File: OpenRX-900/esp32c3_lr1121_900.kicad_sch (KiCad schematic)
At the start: 39 parts, among them U1 ESP32-C3FH4, U2 TLV75533PDQNR, U3 SX1281IMLTRT, U4 RFX2401C, X1 CJ17-400001010B20

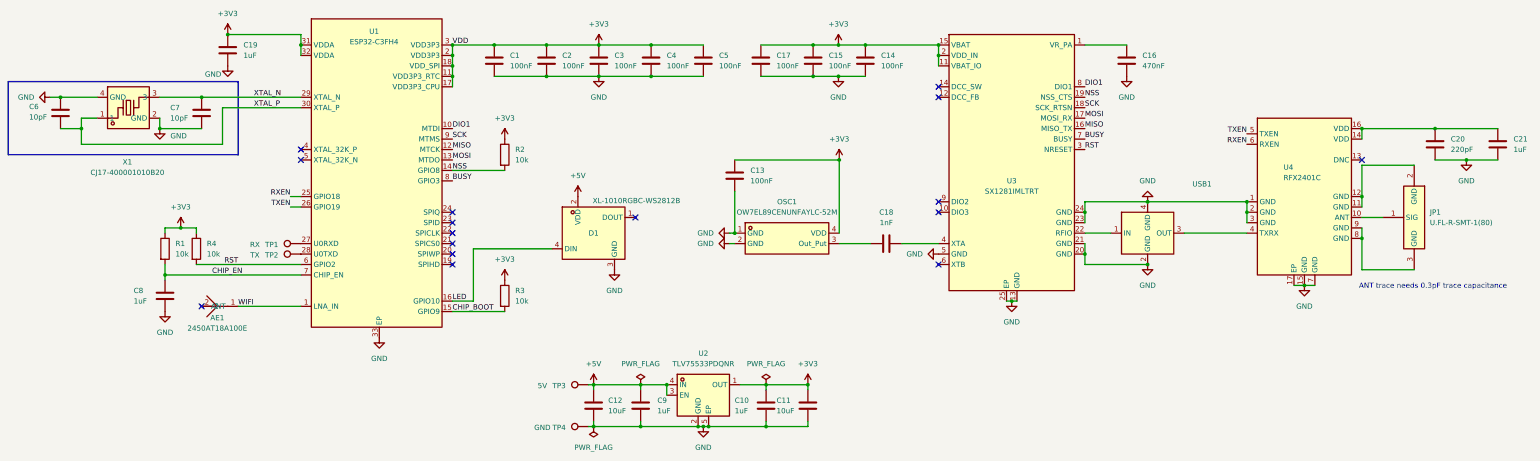
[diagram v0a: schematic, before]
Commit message: OpenRX-900: add all LCSC fields, fix 4.7uF to 0402
- C20 (4.7uF): C23733, footprint fixed from 0201 to 0402
- R5/R6/R7 (100k): C25741, RFSW pull-downs
- L1 (10uH): C1035, 0603 DC-DC inductor
- U4 (LR1121): C7498014
- U5 (32MHz TCXO): C22434888
- T1 (Johanson IPD): C19842466
- JP1 (UFL): C88374
- 0 ERC errors, all components have LCSC fields
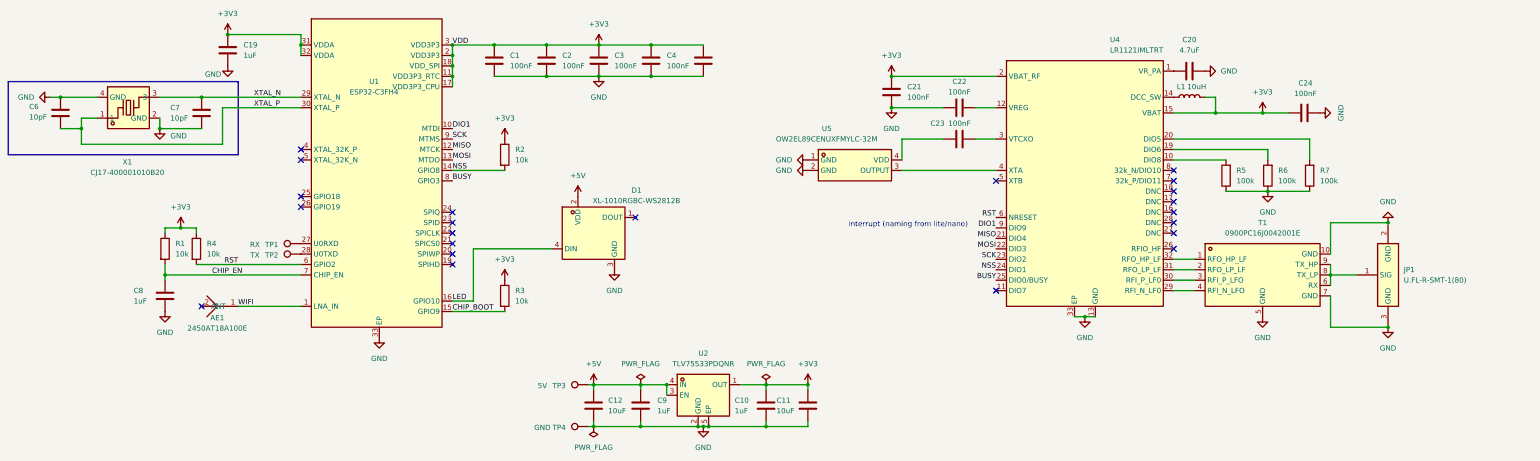
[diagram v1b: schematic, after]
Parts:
- removed C13, C14, C15, C17: 100nF, Capacitor_SMD:C_0201_0603Metric, symbol Device:C
- removed C16: 470nF, Capacitor_SMD:C_0201_0603Metric, symbol Device:C
- removed C18: 1nF, Capacitor_SMD:C_0201_0603Metric, symbol Device:C
- removed OSC1: OW7EL89CENUNFAYLC-52M, OpenRX-Shared:OSC-SMD_4P-L2.0-W1.6-BL_TXC_7Z, symbol OpenRX-Shared:OW7EL89CENUNFAYLC-52M
- removed U3: SX1281IMLTRT, OpenRX-Shared:QFN-24_L4.0-W4.0-P0.50-TL-EP2.6, symbol OpenRX-Shared:SX1281IMLTRT
- removed U4: RFX2401C, OpenRX-Shared:QFN-16_L3.0-W3.0-P0.50-BL-EP1.7, symbol OpenRX-Shared:RFX2401C
- removed USB1: DEA102700LT-6307A2, OpenRX-Shared:FILTER-SMD_4P-L1.0-W0.5-L_DEA102700LT-XXX, symbol OpenRX-Shared:DEA102700LT-6307A2
- added C22, C23, C24: 100nF, Capacitor_SMD:C_0201_0603Metric, symbol Device:C
- added L1: 10uH, Inductor_SMD:L_0603_1608Metric, symbol Device:L
- added R5, R6, R7: 100k, Resistor_SMD:R_0201_0603Metric, symbol Device:R
- added T1: 0900PC16J0042001E, OpenRX-Shared:FILTER-SMD_10P-L2.0-W1.6-BL, symbol OpenRX-Shared:0900PC16J0042001E
- added U4: LR1121IMLTRT, OpenRX-Shared:QFN-32_L5.0-W5.0-P0.50-BL-EP3.7, symbol OpenRX-Shared:LR1121IMLTRT
- added U5: OW2EL89CENUXFMYLC-32M, OpenRX-Shared:OSC-SMD_4P-L3.2-W2.5-BL, symbol OpenRX-Shared:OW2EL89CENUXFMYLC-32M
- C20: value 220pF -> 4.7uF; footprint Capacitor_SMD:C_0201_0603Metric -> Capacitor_SMD:C_0402_1005Metric; LCSC C14856 -> C23733
- C21: value 1uF -> 100nF; LCSC C77857 -> C14858
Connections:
- net +3V3: now also C21.1, C24.2, L1.2, U4.15 (VBAT), U4.2 (VBAT_RF)
- net BUSY: now also U4.25 (DIO0/BUSY)
- net DIO1: now also U4.9 (DIO9)
- net GND: now also JP1.2 (GND), JP1.3 (GND), C22.1, C24.1, R5.1, R6.1, R7.1, T1.10 (GND), T1.5 (GND), T1.7 (GND), U4.13 (GND), U4.33 (EP), U5.1 (GND), U5.2 (GND)
- net MISO: now also U4.21 (DIO4)
- net MOSI: now also U4.22 (DIO3)
- net NSS: now also U4.24 (DIO1)
- net RST: now also U4.6 (NRESET)
- net SCK: now also U4.23 (DIO2)
- net at C20.1: now also U4.1 (VR_PA); no longer C21.1
- net at JP1.1 (SIG): now also T1.6 (RX), T1.8 (TX_LP), T1.9 (TX_HP)
- net RXEN: no longer names the net of U1.25 (GPIO18)
- net TXEN: no longer names the net of U1.26 (GPIO19)
- new net: C22.2, U4.12 (VREG)
- new net: C23.1, U5.4 (VDD)
- new net: C23.2, U4.3 (VTCXO)
- new net: R5.2, U4.10 (DIO8)
- new net: L1.1, U4.14 (DCC_SW)
- new net: R6.2, U4.19 (DIO6)
- new net: R7.2, U4.20 (DIO5)
- new net: T1.4 (RFI_N_LFO), U4.29 (RFI_N_LF0)
- new net: T1.3 (RFI_P_LFO), U4.30 (RFI_P_LF0)
- new net: T1.2 (RFO_LP_LF), U4.31 (RFO_LP_LF)
- new net: T1.1 (RFO_HP_LF), U4.32 (RFO_HP_LF)
- new net: U4.4 (XTA), U5.3 (OUTPUT)
- no-connect marks 16 -> 22
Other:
- note added: "interrupt (naming from lite/nano)"
- note removed: "ANT trace needs 0.3pF trace capacitance"

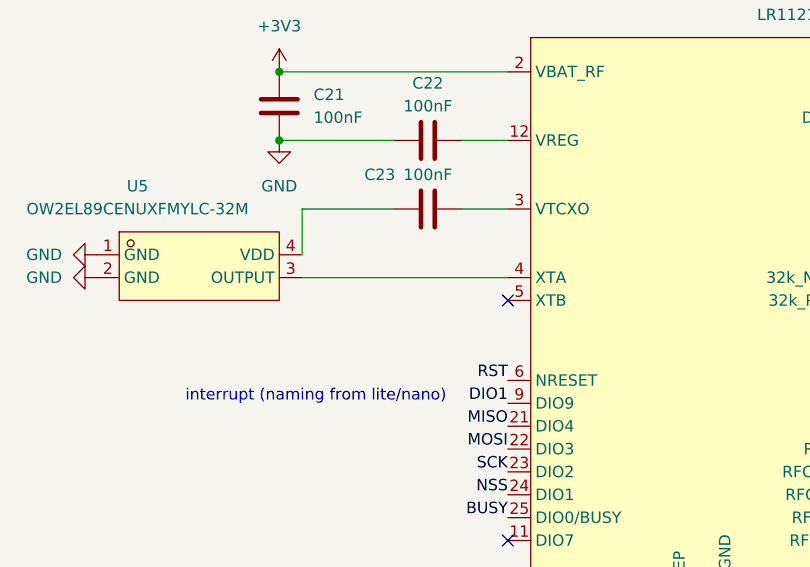
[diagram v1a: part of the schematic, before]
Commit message: Fix 220R LCSC to C25092, add TCXO series resistor to 900
- 220R 0201 1%: C25092 (was incorrectly C25741/100k)
- Both 900 and Dual now have correct 220R + 10pF on TCXO→XTA path
- Nano: RFX2401C VDD now connected to +3V3
- All 4 schematics: 0 ERC errors
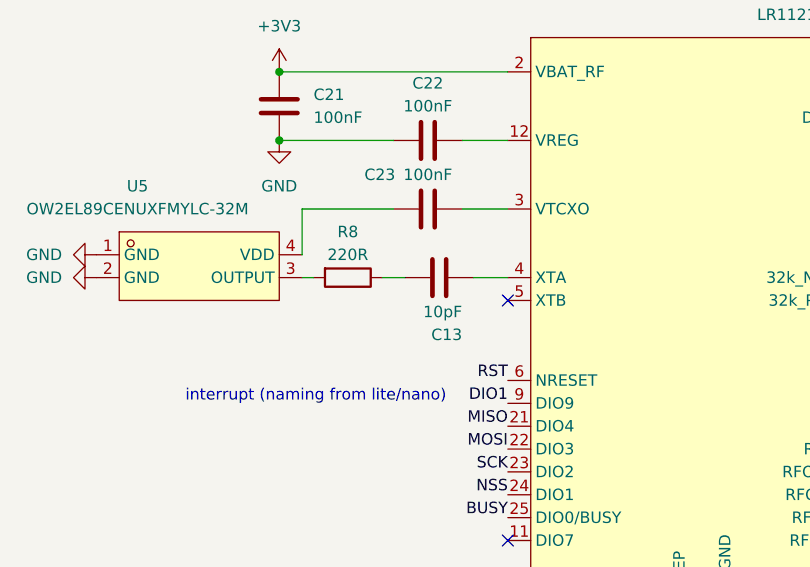
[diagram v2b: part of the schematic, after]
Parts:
- added C13: 10pF, Capacitor_SMD:C_0201_0603Metric, symbol Device:C
- added R8: 220R, Resistor_SMD:R_0201_0603Metric, symbol Device:R
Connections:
- net at U4.4 (XTA): now also C13.2; no longer U5.3 (OUTPUT)
- new net: C13.1, R8.1
- new net: R8.2, U5.3 (OUTPUT)
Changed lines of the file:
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@@
 	(wire
 		(pts
-			(xy 243.84 59.69) (xy 266.7 59.69)
-		)
-		(stroke
-			(width 0)
-			(type default)
-		)
-	)
-	(wire
-		(pts
 			(xy 309.88 86.36) (xy 314.96 86.36)
 		)
@@
 	(wire
 		(pts
+			(xy 245.11 59.69) (xy 243.84 59.69)
+		)
+		(stroke
+			(width 0)
+			(type default)
+		)
+	)
+	(wire
+		(pts
 			(xy 309.88 83.82) (xy 314.96 83.82)
 		)
@@
 	(wire
 		(pts
+			(xy 252.73 59.69) (xy 255.27 59.69)
+		)
+		(stroke
+			(width 0)
+			(type default)
+		)
+	)
+	(wire
+		(pts
 			(xy 64.77 85.09) (xy 64.77 82.55)
 		)
@@
 	(wire
 		(pts
+			(xy 262.89 59.69) (xy 266.7 59.69)
+		)
+		(stroke
+			(width 0)
+			(type default)
+		)
+	)
+	(wire
+		(pts
 			(xy 167.64 111.76) (xy 180.34 111.76)
 		)
@@
 			)
 		)
-		(pin "3"
-		)
-		(pin "2"
-		)
 		(property "LCSC" "C88374"
 			(at 0 0 0)
+			(hide yes)
 			(show_name no)
 			(do_not_autoplace no)
-			(hide yes)
 			(effects
 				(font
@@
 			)
 		)
+		(pin "3"
+		)
+		(pin "2"
+		)
 		(pin "1"
 		)
@@
 			)
 		)
-		(pin "2"
-		)
-		(pin "6"
-		)
-		(pin "7"
-		)
-		(pin "9"
-		)
-		(pin "5"
-		)
 		(property "LCSC" "C7498014"
 			(at 0 0 0)
+			(hide yes)
 			(show_name no)
 			(do_not_autoplace no)
-			(hide yes)
 			(effects
 				(font
@@
 			)
 		)
+		(pin "2"
+		)
+		(pin "6"
+		)
+		(pin "7"
+		)
+		(pin "9"
+		)
+		(pin "5"
+		)
 		(pin "1"
 		)
@@
 		(property "LCSC" "C23733"
 			(at 0 0 0)
+			(hide yes)
 			(show_name no)
 			(do_not_autoplace no)
-			(hide yes)
 			(effects
 				(font
@@
 	)
 	(symbol
+		(lib_id "Device:C")
+		(at 259.08 59.69 90)
+		(unit 1)
+		(body_style 1)
+		(exclude_from_sim no)
+		(in_bom yes)
+		(on_board yes)
+		(in_pos_files yes)
+		(dnp no)
+		(property "Reference" "C13"
+			(at 261.62 66.04 90)
+			(show_name no)
+			(do_not_autoplace no)
+			(effects
+				(font
+					(size 1.27 1.27)
+				)
+				(justify left)
+			)
+		)
+		(property "Value" "10pF"
+			(at 261.62 63.5 90)
+			(show_name no)
+			(do_not_autoplace no)
+			(effects
+				(font
+					(size 1.27 1.27)
+				)
+				(justify left)
+			)
+		)
+		(property "Footprint" "Capacitor_SMD:C_0201_0603Metric"
+			(at 262.89 58.7248 0)
+			(hide yes)
+			(show_name no)
+			(do_not_autoplace no)
+			(effects
+				(font
+					(size 1.27 1.27)
+				)
+			)
+		)
+		(property "Datasheet" ""
+			(at 259.08 59.69 0)
+			(hide yes)
+			(show_name no)
+			(do_not_autoplace no)
+			(effects
+				(font
+					(size 1.27 1.27)
+				)
+			)
+		)
+		(property "Description" "Unpolarized capacitor"
+			(at 259.08 59.69 0)
+			(hide yes)
+			(show_name no)
+			(do_not_autoplace no)
+			(effects
+				(font
+					(size 1.27 1.27)
+				)
+			)
+		)
+		(property "LCSC" "C14854"
+			(at 213.36 133.35 0)
+			(hide yes)
+			(show_name no)
+			(do_not_autoplace no)
+			(effects
+				(font
+					(size 1.27 1.27)
+				)
+			)
+		)
+		(pin "1"
+		)
+		(pin "2"
+		)
+		(instances
+			(project "OpenRX-900"
+				(path "/a1b2c3d4-e5f6-7890-abcd-ef1234567890/e1f2a3b4-c5d6-7890-1234-567890abcdef"
+					(reference "C13")
+					(unit 1)
+				)
+			)
+		)
+	)
+	(symbol
 		(lib_id "power:GND")
 		(at 331.47 95.25 0)
@@
 			)
 		)
-		(pin "4"
-		)
-		(pin "3"
-		)
 		(property "LCSC" "C22434888"
 			(at 0 0 0)
+			(hide yes)
 			(show_name no)
 			(do_not_autoplace no)
-			(hide yes)
 			(effects
 				(font
@@
 			)
 		)
+		(pin "4"
+		)
+		(pin "3"
+		)
 		(pin "1"
 		)
@@
 			)
 		)
+		(property "LCSC" "C1035"
+			(at 0 0 0)
+			(hide yes)
+			(show_name no)
+			(do_not_autoplace no)
+			(effects
+				(font
+					(size 1.27 1.27)
+				)
+			)
+		)
 		(pin "2"
 		)
-		(property "LCSC" "C1035"
+		(pin "1"
+		)
+		(instances
+			(project "OpenRX-900"
+				(path "/a1b2c3d4-e5f6-7890-abcd-ef1234567890/e1f2a3b4-c5d6-7890-1234-567890abcdef"
+					(reference "L1")
+					(unit 1)
+				)
+			)
+		)
+	)
+	(symbol
+		(lib_id "Device:R")
+		(at 248.92 59.69 270)
+		(unit 1)
+		(body_style 1)
+		(exclude_from_sim no)
+		(in_bom yes)
+		(on_board yes)
+		(in_pos_files yes)
+		(dnp no)
+		(property "Reference" "R8"
+			(at 248.92 54.61 90)
+			(show_name no)
+			(do_not_autoplace no)
+			(effects
+				(font
+					(size 1.27 1.27)
+				)
+			)
+		)
+		(property "Value" "220R"
+			(at 248.92 57.15 90)
+			(show_name no)
+			(do_not_autoplace no)
+			(effects
+				(font
+					(size 1.27 1.27)
+				)
+			)
+		)
+		(property "Footprint" "Resistor_SMD:R_0201_0603Metric"
+			(at 248.92 57.912 90)
+			(hide yes)
+			(show_name no)
+			(do_not_autoplace no)
+			(effects
+				(font
+					(size 1.27 1.27)
+				)
+			)
+		)
+		(property "Datasheet" ""
+			(at 248.92 59.69 0)
+			(hide yes)
+			(show_name no)
+			(do_not_autoplace no)
+			(effects
+				(font
+					(size 1.27 1.27)
+				)
+			)
+		)
+		(property "Description" "Resistor"
+			(at 248.92 59.69 0)
+			(hide yes)
+			(show_name no)
+			(do_not_autoplace no)
+			(effects
+				(font
+					(size 1.27 1.27)
+				)
+			)
+		)
+		(property "LCSC" "C25092"
+			(at 187.96 382.27 0)
+			(hide yes)
+			(show_name no)
+			(do_not_autoplace no)
+			(effects
+				(font
+					(size 1.27 1.27)
+				)
+			)
+		)
+		(property "LCSC" "C25092"
 			(at 0 0 0)
 			(show_name no)
@@
 			)
 		)
+		(pin "2"
+		)
 		(pin "1"
 		)
@@
 			(project "OpenRX-900"
 				(path "/a1b2c3d4-e5f6-7890-abcd-ef1234567890/e1f2a3b4-c5d6-7890-1234-567890abcdef"
-					(reference "L1")
+					(reference "R8")
 					(unit 1)
 				)
@@
 			)
 		)
+		(property "LCSC" "C19842466"
+			(at 0 0 0)
+			(hide yes)
+			(show_name no)
+			(do_not_autoplace no)
+			(effects
+				(font
+					(size 1.27 1.27)
+				)
+			)
+		)
 		(pin "4"
 		)
@@
 		(pin "8"
 		)
-		(property "LCSC" "C19842466"
-			(at 0 0 0)
-			(show_name no)
-			(do_not_autoplace no)
-			(hide yes)
-			(effects
-				(font
-					(size 1.27 1.27)
-				)
-			)
-		)
 		(pin "1"
 		)
@@
 			)
 		)
-		(pin "2"
-		)
 		(property "LCSC" "C25741"
 			(at 0 0 0)
+			(hide yes)
 			(show_name no)
 			(do_not_autoplace no)
-			(hide yes)
 			(effects
 				(font
@@
 			)
 		)
+		(pin "2"
+		)
 		(pin "1"
 		)
@@
 			)
 		)
-		(pin "2"
-		)
 		(property "LCSC" "C25741"
 			(at 0 0 0)
+			(hide yes)
 			(show_name no)
 			(do_not_autoplace no)
-			(hide yes)
 			(effects
 				(font
@@
 			)
 		)
+		(pin "2"
+		)
 		(pin "1"
 		)
@@
 			)
 		)
-		(pin "2"
-		)
 		(property "LCSC" "C25741"
 			(at 0 0 0)
+			(hide yes)
 			(show_name no)
 			(do_not_autoplace no)
-			(hide yes)
 			(effects
 				(font
@@
 			)
 		)
+		(pin "2"
+		)
 		(pin "1"

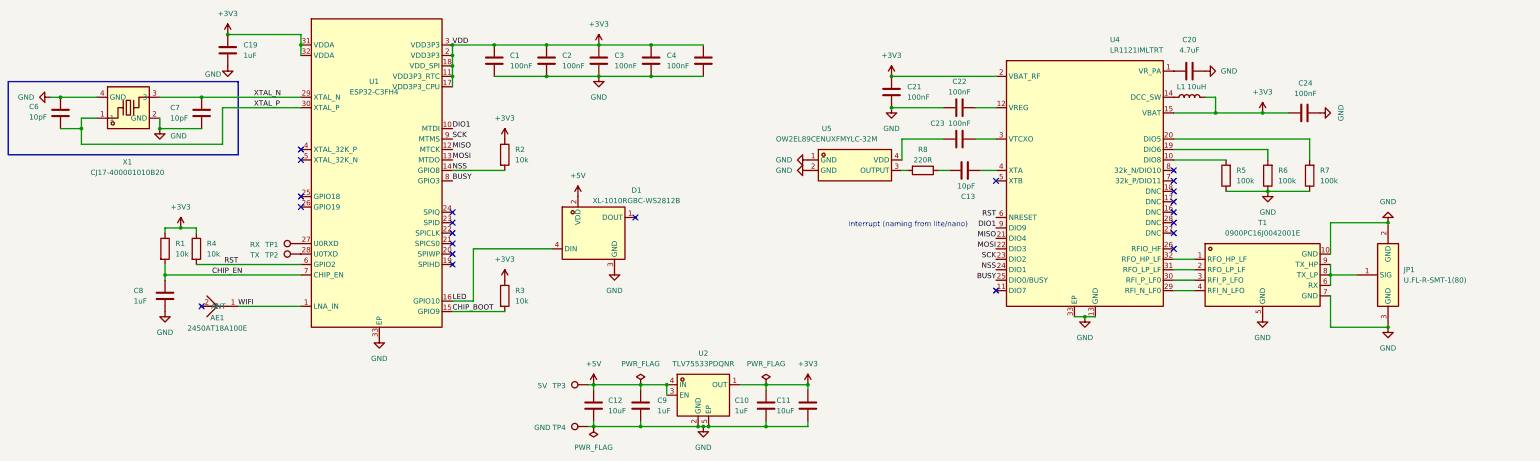
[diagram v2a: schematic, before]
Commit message: Fix crystal load caps: 10pF → 18pF (C71153) on all 4 receivers
CJ17-400001010B20 crystal has CL=10pF. With 10pF load caps and
~2pF stray, effective load was only 7pF (30% low). Changed to 18pF
giving ~11pF effective load, matching the crystal spec.

C71153 = Samsung CL03C180JA3NNNC, 18pF C0G 25V 0201.
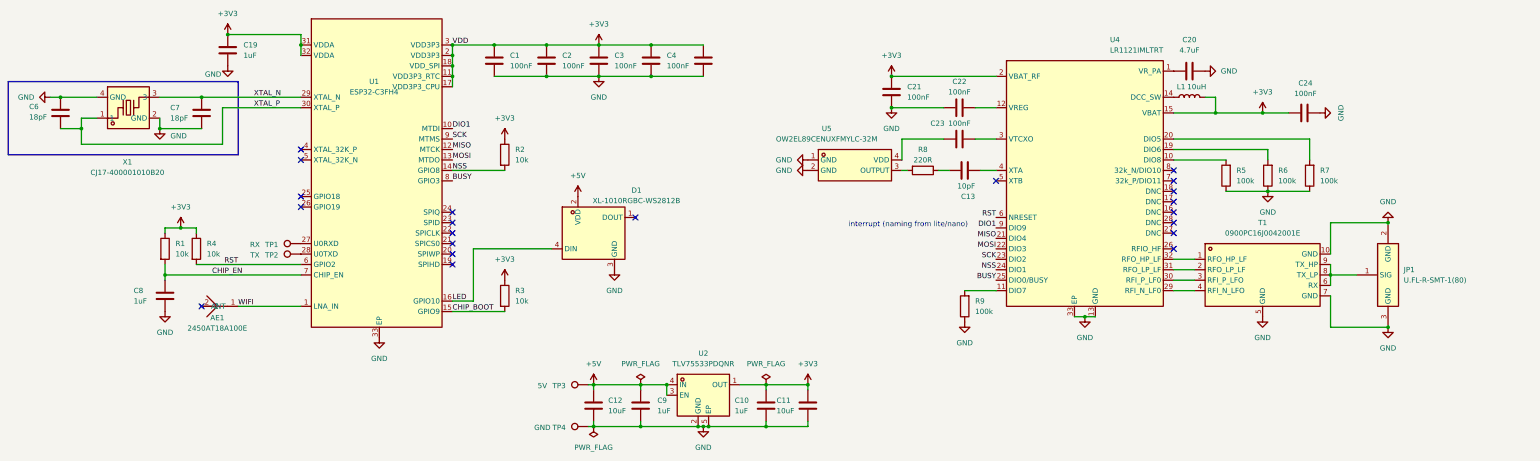
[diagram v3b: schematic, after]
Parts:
- added R9: 100k, Resistor_SMD:R_0201_0603Metric, symbol Device:R
- C6, C7: value 10pF -> 18pF; LCSC C14854 -> C71153
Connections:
- net GND: now also R9.1
- net at U4.11 (DIO7): now also R9.2
- no-connect marks 22 -> 21
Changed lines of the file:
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@@
 	)
 	(no_connect
-		(at 266.7 88.9)
-	)
-	(no_connect
 		(at 309.88 67.31)
 	)
@@
 	(wire
 		(pts
+			(xy 259.08 88.9) (xy 266.7 88.9)
+		)
+		(stroke
+			(width 0)
+			(type default)
+		)
+	)
+	(wire
+		(pts
 			(xy 180.34 121.92) (xy 194.31 121.92)
 		)
@@
 			)
 		)
-		(property "Value" "10pF"
+		(property "Value" "18pF"
 			(at 66.04 46.99 0)
 			(show_name no)
@@
 			)
 		)
-		(property "LCSC" "C14854"
+		(property "LCSC" "C71153"
 			(at 0 0 0)
 			(hide yes)
@@
 			)
 		)
-		(property "Value" "10pF"
+		(property "Value" "18pF"
 			(at 31.75 46.736 0)
 			(show_name no)
@@
 			)
 		)
-		(property "LCSC" "C14854"
+		(property "LCSC" "C71153"
 			(at 0 0 0)
 			(hide yes)
@@
 		)
 		(property "LCSC" "C25092"
-			(at 187.96 382.27 0)
+			(at 0 0 0)
 			(hide yes)
 			(show_name no)
@@
 			)
 		)
-		(property "LCSC" "C25092"
-			(at 0 0 0)
+		(pin "2"
+		)
+		(pin "1"
+		)
+		(instances
+			(project "OpenRX-900"
+				(path "/a1b2c3d4-e5f6-7890-abcd-ef1234567890/e1f2a3b4-c5d6-7890-1234-567890abcdef"
+					(reference "R8")
+					(unit 1)
+				)
+			)
+		)
+	)
+	(symbol
+		(lib_id "power:GND")
+		(at 259.08 96.52 0)
+		(unit 1)
+		(body_style 1)
+		(exclude_from_sim no)
+		(in_bom yes)
+		(on_board yes)
+		(in_pos_files yes)
+		(dnp no)
+		(fields_autoplaced yes)
+		(property "Reference" "#PWR041"
+			(at 259.08 102.87 0)
+			(hide yes)
 			(show_name no)
 			(do_not_autoplace no)
+			(effects
+				(font
+					(size 1.27 1.27)
+				)
+			)
+		)
+		(property "Value" "GND"
+			(at 259.08 101.6 0)
+			(show_name no)
+			(do_not_autoplace no)
+			(effects
+				(font
+					(size 1.27 1.27)
+				)
+			)
+		)
+		(property "Footprint" ""
+			(at 259.08 96.52 0)
 			(hide yes)
+			(show_name no)
+			(do_not_autoplace no)
 			(effects
 				(font
@@
 			)
 		)
-		(pin "2"
+		(property "Datasheet" ""
+			(at 259.08 96.52 0)
+			(hide yes)
+			(show_name no)
+			(do_not_autoplace no)
+			(effects
+				(font
+					(size 1.27 1.27)
+				)
+			)
+		)
+		(property "Description" "Power symbol creates a global label with name \"GND\" , ground"
+			(at 259.08 96.52 0)
+			(hide yes)
+			(show_name no)
+			(do_not_autoplace no)
+			(effects
+				(font
+					(size 1.27 1.27)
+				)
+			)
 		)
 		(pin "1"
@@
 			(project "OpenRX-900"
 				(path "/a1b2c3d4-e5f6-7890-abcd-ef1234567890/e1f2a3b4-c5d6-7890-1234-567890abcdef"
-					(reference "R8")
+					(reference "#PWR041")
 					(unit 1)
 				)
@@
 					(unit 1)
 				)
+			)
+		)
+	)
+	(symbol
+		(lib_id "Device:R")
+		(at 259.08 92.71 180)
+		(unit 1)
+		(body_style 1)
+		(exclude_from_sim no)
+		(in_bom yes)
+		(on_board yes)
+		(in_pos_files yes)
+		(dnp no)
+		(fields_autoplaced yes)
+		(property "Reference" "R9"
+			(at 261.62 91.4399 0)
+			(show_name no)
+			(do_not_autoplace no)
+			(effects
+				(font
+					(size 1.27 1.27)
+				)
+				(justify right)
+			)
+		)
+		(property "Value" "100k"
+			(at 261.62 93.9799 0)
+			(show_name no)
+			(do_not_autoplace no)
+			(effects
+				(font
+					(size 1.27 1.27)
+				)
+				(justify right)
+			)
+		)
+		(property "Footprint" "Resistor_SMD:R_0201_0603Metric"
+			(at 260.858 92.71 90)
+			(hide yes)
+			(show_name no)
+			(do_not_autoplace no)
+			(effects
+				(font
+					(size 1.27 1.27)
+				)
+			)
+		)
+		(property "Datasheet" ""
+			(at 259.08 92.71 0)
+			(hide yes)
+			(show_name no)
+			(do_not_autoplace no)
+			(effects
+				(font
+					(size 1.27 1.27)
+				)
+			)
+		)
+		(property "Description" "Resistor"
+			(at 259.08 92.71 0)
+			(hide yes)
+			(show_name no)
+			(do_not_autoplace no)
+			(effects
+				(font
+					(size 1.27 1.27)
+				)
+			)
+		)
+		(property "LCSC" "C25741"
+			(at -63.5 31.75 0)
+			(hide yes)
+			(show_name no)
+			(do_not_autoplace no)
+			(effects
+				(font
+					(size 1.27 1.27)
+				)
+			)
+		)
+		(pin "2"
+		)
+		(pin "1"
+		)
+		(instances
+			(project "OpenRX-900"
+				(path "/a1b2c3d4-e5f6-7890-abcd-ef1234567890/e1f2a3b4-c5d6-7890-1234-567890abcdef"
+					(reference "R9")
+					(unit 1)
+				)
